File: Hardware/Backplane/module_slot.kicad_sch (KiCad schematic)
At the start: 31 parts, among them J201 Conn_01x10, J202 10018784-10201TLF, J203 Conn_01x06, Q201 NMOS, Q202 PMOS, Q203 PMOS, Q204 PMOS, U201 CH32V003FxPx

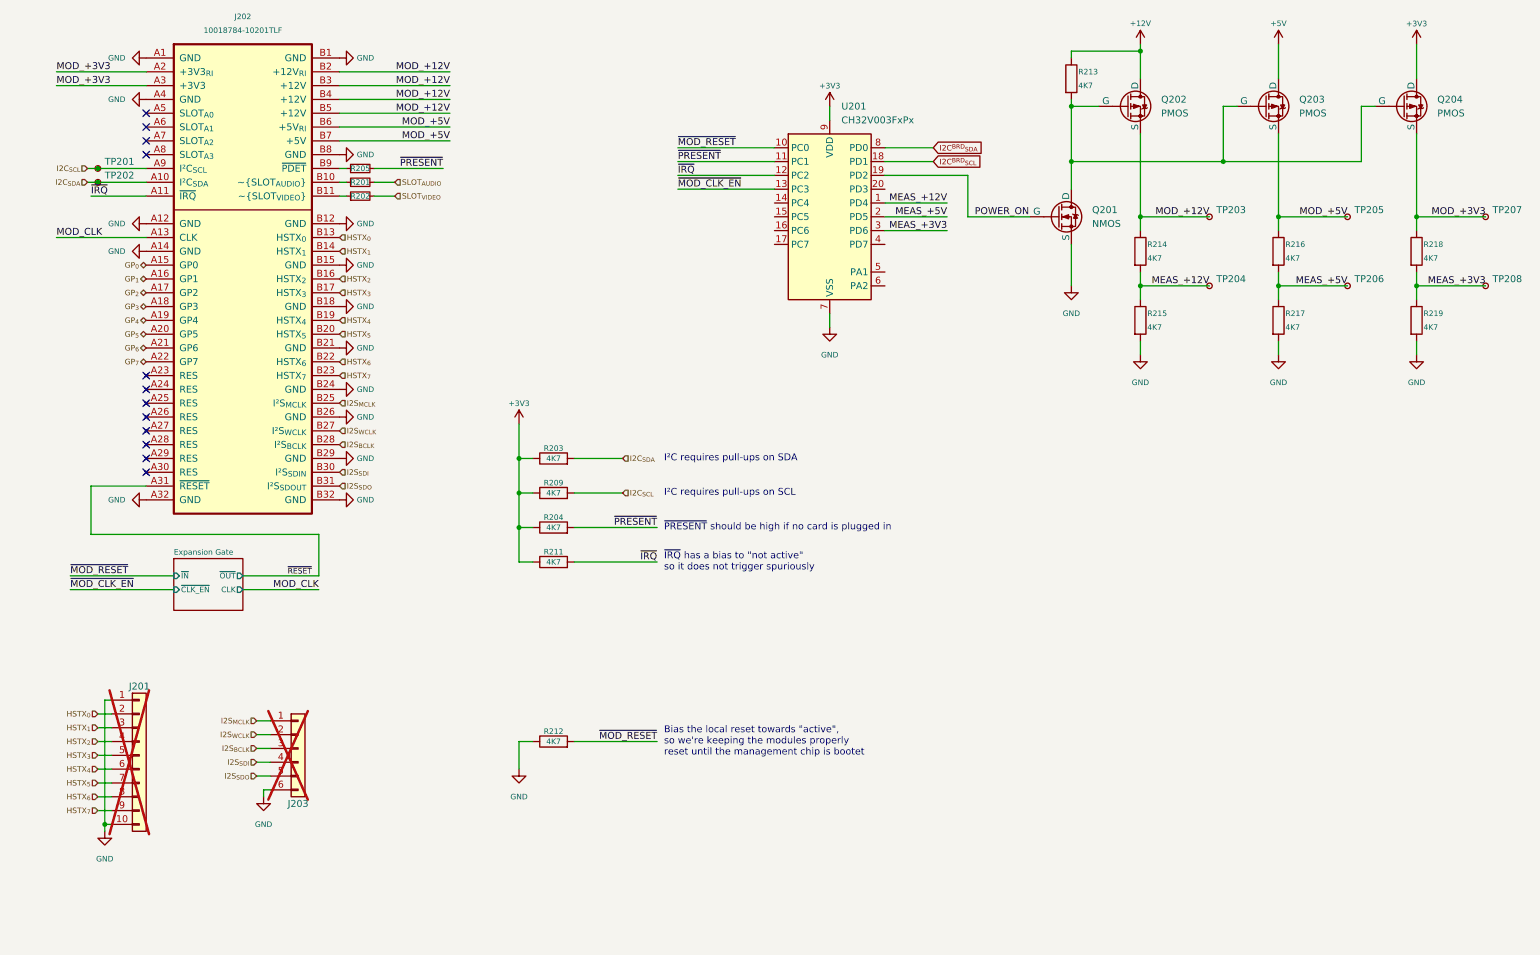
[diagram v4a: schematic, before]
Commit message: Starts to implement a tool to generate symbols for KiCAD from a generic description.
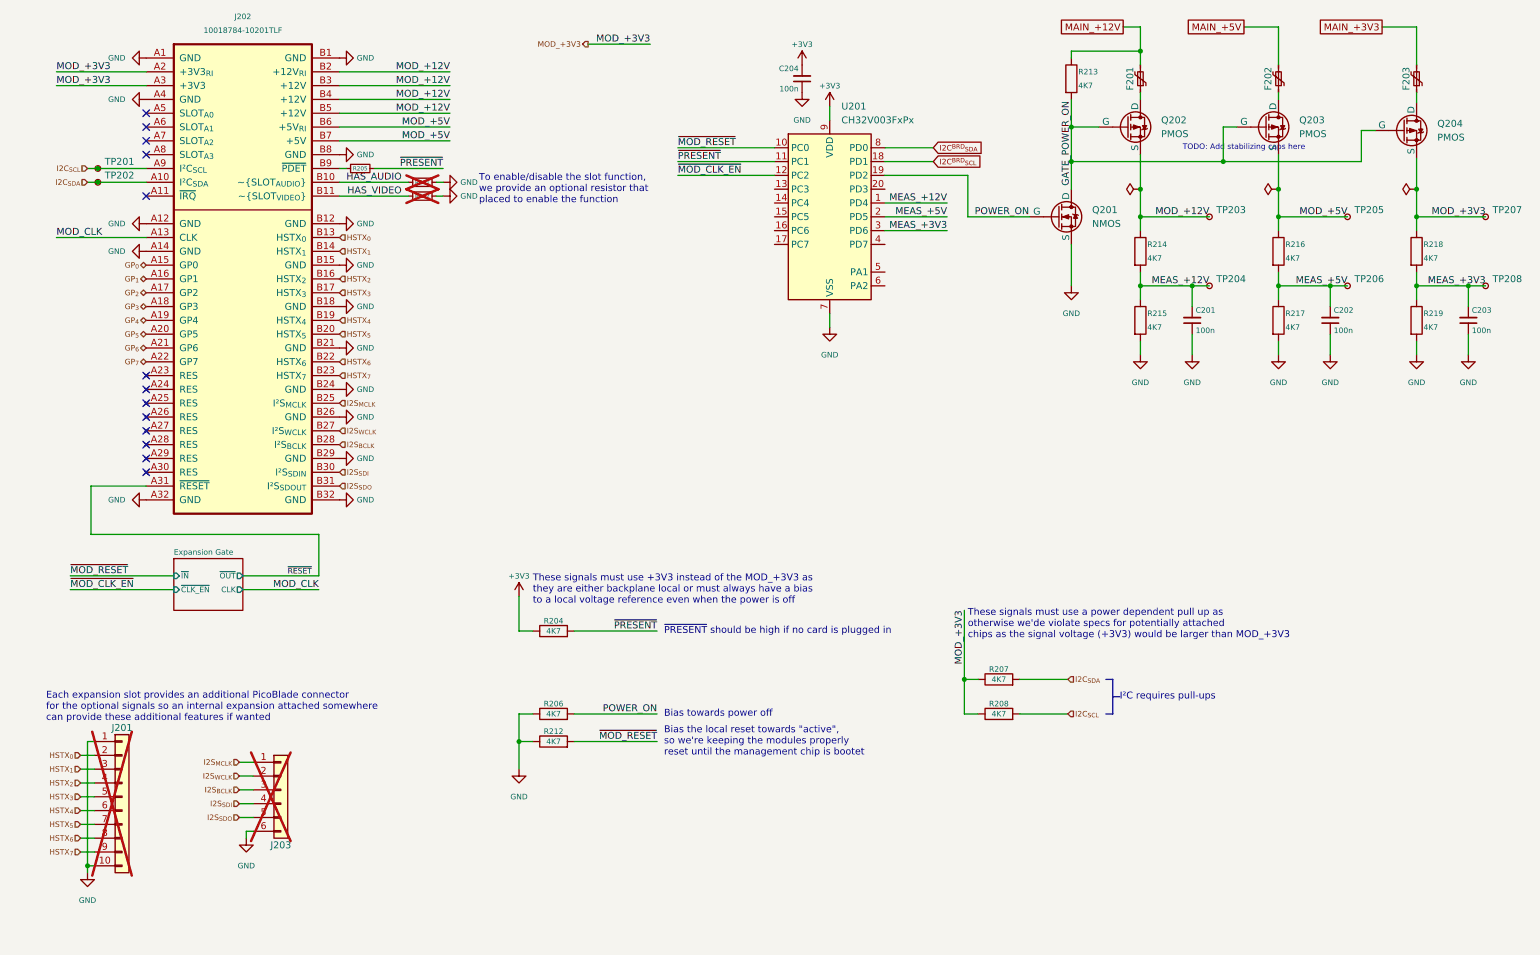
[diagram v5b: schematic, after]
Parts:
- removed R203, R209, R211: 4K7, Resistor_SMD:R_0603_1608Metric, symbol Device:R
- added C201, C202, C203, C204: 100n, Capacitor_SMD:C_0603_1608Metric, symbol Device:C_Small
- added F201, F202, F203: SMD1206B050TF/15, symbol Symbol Library:SMD1206B050TF/15
- added R206, R207, R208: 4K7, Resistor_SMD:R_0603_1608Metric, symbol Device:R
- R201, R202: value 1K -> 0; now not fitted
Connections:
- net SLOT_{AUDIO} is gone; now on net GND: R201.2
- net SLOT_{VIDEO} is gone; now on net GND: R202.2
- net +3V3: now also C204.2; no longer Q204.1 (D)
- net GND: now also C201.1, C202.1, C203.1, C204.1, R206.1
- net I2C_{SCL}: now also R208.2
- net I2C_{SDA}: now also R207.2
- net MEAS_+12V: now also C201.2
- net MEAS_+3V3: now also C203.2
- net MEAS_+5V: now also C202.2
- net MOD_+3V3: now also R207.1, R208.1
- net POWER_ON: now also R206.2
- net ~{MOD_CLK_EN}: now also U201.12 (PC2); no longer U201.13 (PC3)
- net GATE_POWER_ON: now reaches Q201.1 (D), Q202.2 (G), Q203.2 (G), Q204.2 (G), R213.2
- net HAS_VIDEO: now reaches J202.B11 (~{SLOT_{VIDEO}}), R202.1
- net HAS_AUDIO: now reaches J202.B10 (~{SLOT_{AUDIO}}), R201.1
- net +12V: no longer names the net of Q202.1 (D)
- net +12V: now also F201.1; no longer R213.1
- net +5V: no longer names the net of Q203.1 (D)
- net +5V: now also F202.1
- net ~{IRQ}: no longer names the net of J202.A11 (~{IRQ})
- net ~{IRQ}: no longer U201.12 (PC2)
- new net: F203.1, Q204.1 (D)
- new net MAIN_+12V: F201.2, R213.1
- new net MAIN_+3V3: F203.2
- new net MAIN_+5V: F202.2
- no-connect marks 12 -> 13
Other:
- note added: "Bias towards power off"
- note added: "Each expansion slot provides an additional PicoBlade connector for the optional signals so an internal expansion attached somewhere can provide these additional features if wanted"
- note added: "I²C requires pull-ups"
- note added: "TODO: Add stabilizing caps here"
- note added: "These signals must use +3V3 instead of the MOD_+3V3 as they are either backplane local or must always have a bias to a local voltage reference even when the power is off"
- note added: "These signals must use a power dependent pull up as otherwise we'de violate specs for potentially attached chips as the signal voltage (+3V3) would be larger than MOD_+3V3"
- note added: "To enable/disable the slot function, we provide an optional resistor that placed to enable the function"
- note removed: "I²C requires pull-ups on SCL"
- note removed: "I²C requires pull-ups on SDA"
- note removed: "~{IRQ} has a bias to "not active" so it does not trigger spuriously"
- moved on the sheet: J201, J203, Q202, Q203, Q204, R204

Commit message: Cleans up the backplane schematic and improves on features a lot.
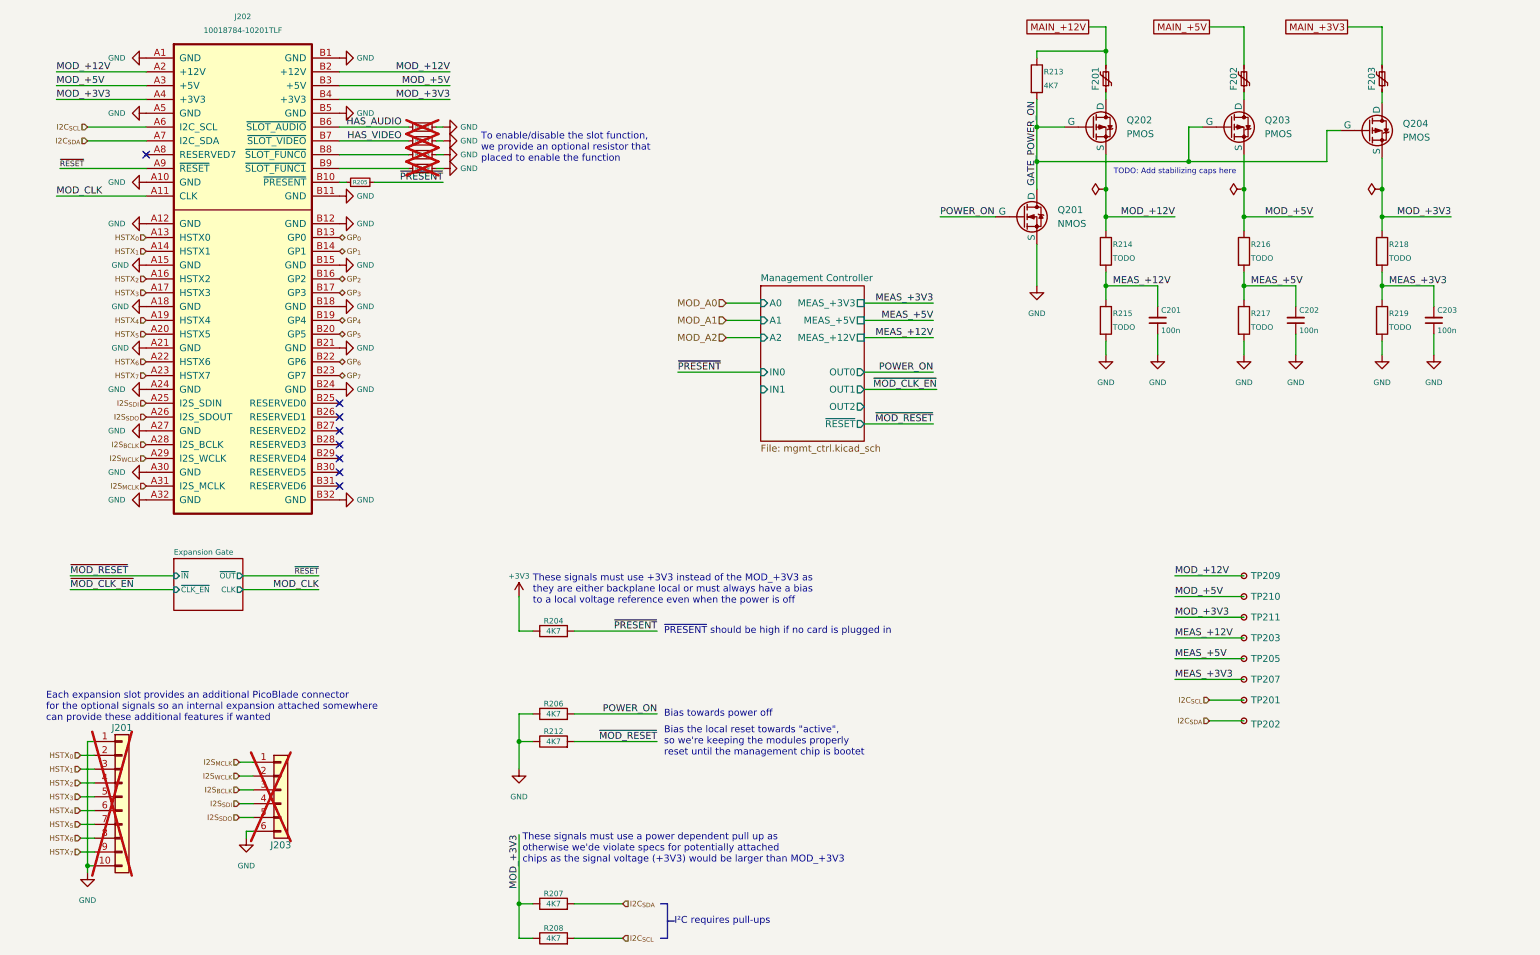
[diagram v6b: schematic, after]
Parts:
- removed C204: 100n, Capacitor_SMD:C_0603_1608Metric, symbol Device:C_Small
- removed TP204, TP206, TP208: TestPoint_Small, TestPoint:TestPoint_Pad_D1.0mm, symbol Connector:TestPoint_Small
- removed U201: CH32V003FxPx, Package_SO:TSSOP-20_4.4x6.5mm_P0.65mm, symbol MCU_WCH_CH32V0:CH32V003FxPx
- added R203, R209: 0, Resistor_SMD:R_0603_1608Metric, symbol Device:R_Small
- added TP209, TP210, TP211: TestPoint_Small, TestPoint:TestPoint_Pad_D1.0mm, symbol Connector:TestPoint_Small
- J202: MANUFACTURER AMPHENOL -> (none); PARTREV A -> (none); STANDARD MANUFACTURER RECOMMENDATIONS -> (none)
- R214, R215, R216, R217, R218, R219: value 4K7 -> TODO
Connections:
- net GND: now also J202.A10 (GND), J202.A15 (GND), J202.A18 (GND), J202.A21 (GND), J202.A24 (GND), J202.A27 (GND), J202.A30 (GND), J202.A5 (GND), J202.B11 (GND), J202.B5 (GND), R203.2, R209.2; no longer J202.A14 (GND), J202.A4 (GND), J202.B26 (GND), J202.B29 (GND), J202.B8 (GND)
- net GP_{0}: now also J202.B13 (GP0); no longer J202.A15 (GP0)
- net GP_{1}: now also J202.B14 (GP1); no longer J202.A16 (GP1)
- net GP_{2}: now also J202.B16 (GP2); no longer J202.A17 (GP2)
- net GP_{3}: now also J202.B17 (GP3); no longer J202.A18 (GP3)
- net GP_{4}: now also J202.B19 (GP4); no longer J202.A19 (GP4)
- net GP_{5}: now also J202.B20 (GP5); no longer J202.A20 (GP5)
- net GP_{6}: now also J202.B22 (GP6); no longer J202.A21 (GP6)
- net GP_{7}: now also J202.B23 (GP7); no longer J202.A22 (GP7)
- net HAS_AUDIO: now also J202.B6 (~{SLOT_AUDIO}); no longer J202.B10 (~{SLOT_{AUDIO}})
- net HAS_VIDEO: now also J202.B7 (~{SLOT_VIDEO}); no longer J202.B11 (~{SLOT_{VIDEO}})
- net HSTX_{0}: now also J202.A13 (HSTX0); no longer J202.B13 (HSTX_{0})
- net HSTX_{1}: now also J202.A14 (HSTX1); no longer J202.B14 (HSTX_{1})
- net HSTX_{2}: now also J202.A16 (HSTX2); no longer J202.B16 (HSTX_{2})
- net HSTX_{3}: now also J202.A17 (HSTX3); no longer J202.B17 (HSTX_{3})
- net HSTX_{4}: now also J202.A19 (HSTX4); no longer J202.B19 (HSTX_{4})
- net HSTX_{5}: now also J202.A20 (HSTX5); no longer J202.B20 (HSTX_{5})
- net HSTX_{6}: now also J202.A22 (HSTX6); no longer J202.B22 (HSTX_{6})
- net HSTX_{7}: now also J202.A23 (HSTX7); no longer J202.B23 (HSTX_{7})
- net I2C_{SCL}: now also J202.A6 (I2C_SCL); no longer J202.A9 (I²C_{SCL})
- net I2C_{SDA}: now also J202.A7 (I2C_SDA); no longer J202.A10 (I²C_{SDA})
- net I2S_{BCLK}: now also J202.A28 (I2S_BCLK); no longer J202.B28 (I²S_{BCLK})
- net I2S_{MCLK}: now also J202.A31 (I2S_MCLK); no longer J202.B25 (I²S_{MCLK})
- net I2S_{SDI}: now also J202.A25 (I2S_SDIN); no longer J202.B30 (I²S_{SDIN})
- net I2S_{SDO}: now also J202.A26 (I2S_SDOUT); no longer J202.B31 (I²S_{SDOUT})
- net I2S_{WCLK}: now also J202.A29 (I2S_WCLK); no longer J202.B27 (I²S_{WCLK})
- net MEAS_+12V: now also TP203.1
- net MEAS_+3V3: now also TP207.1
- net MEAS_+5V: now also TP205.1
- net MOD_+12V: now also J202.A2 (+12V), TP209.1; no longer J202.B3 (+12V), J202.B4 (+12V), J202.B5 (+12V), TP203.1
- net MOD_+3V3: now also J202.A4 (+3V3), J202.B4 (+3V3), TP211.1; no longer J202.A2 (+3V3_{RI}), J202.A3 (+3V3), TP207.1
- net MOD_+5V: now also J202.A3 (+5V), J202.B3 (+5V), TP210.1; no longer J202.B6 (+5V_{RI}), J202.B7 (+5V), TP205.1
- net MOD_CLK: now also J202.A11 (CLK); no longer J202.A13 (CLK)
- net ~{RESET}: now also J202.A9 (~{RESET}); no longer J202.A31 (~{RESET})
- net at J202.B9 (~{SLOT_FUNC1}): now also R209.1; no longer R205.1
- new net: J202.B10 (~{PRESENT}), R205.1
- new net: J202.B8 (~{SLOT_FUNC0}), R203.1
- no-connect marks 13 -> 8
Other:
- added sheet Management Controller (mgmt_ctrl.kicad_sch)
- moved on the sheet: C201, C202, C203, F201, F202, F203, Q201, Q202, Q203, Q204, R201, R202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

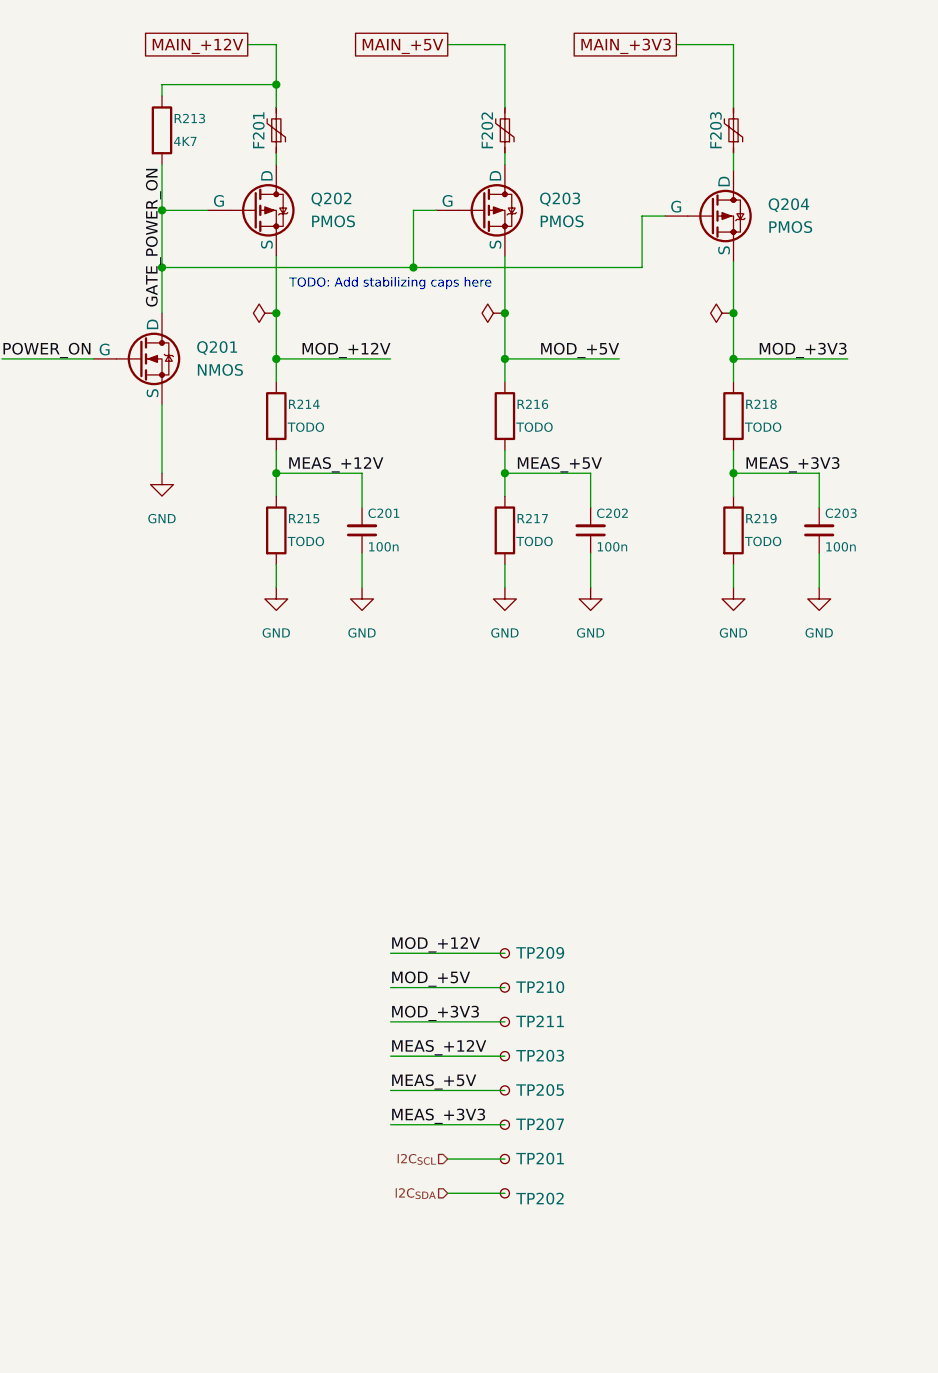
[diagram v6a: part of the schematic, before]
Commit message: Cleans up schematic, adds clean RESET gating
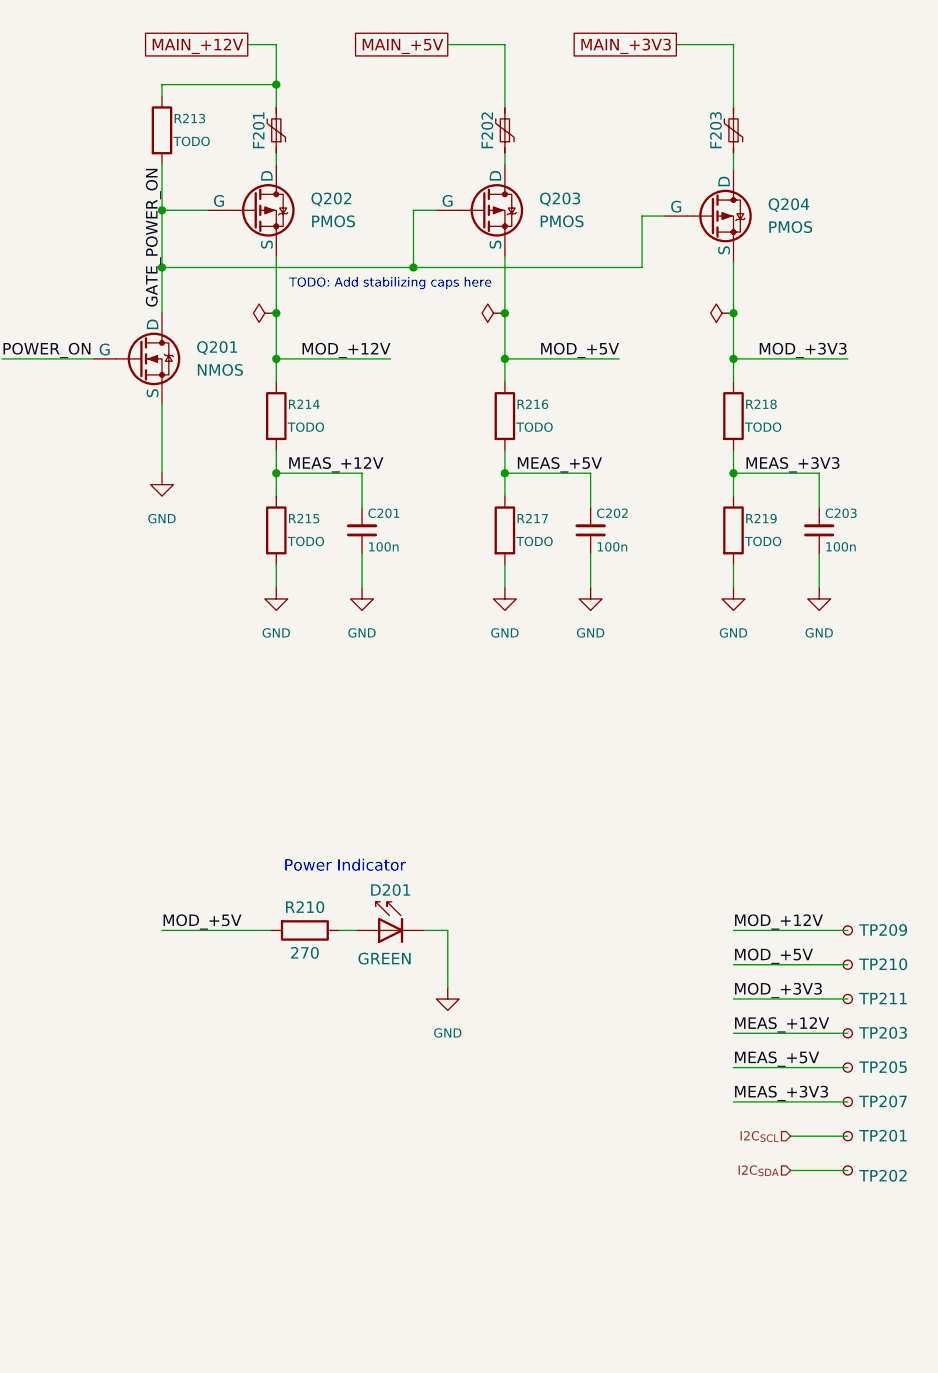
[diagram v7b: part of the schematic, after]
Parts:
- added D201: GREEN, LED_SMD:LED_0603_1608Metric, symbol LED:LD271
- added R210: 270, symbol Device:R
- R213: value 4K7 -> TODO
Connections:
- net GND: now also D201.1 (K)
- net MOD_+5V: now also R210.2
- new net: D201.2 (A), R210.1
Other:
- note added: "Power Indicator"
- company: (none) -> Ashet Technologies
- title: (none) -> Expansion Port
- moved on the sheet: TP201, TP202, TP203, TP205, TP207, TP209, TP210, TP211
